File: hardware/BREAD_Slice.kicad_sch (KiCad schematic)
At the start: 29 parts, among them J1 I2C_01x04, J2 Conn_01x10_Female, K2 SANYOU_SRD_Form_C, Q1 IRLZ34N, Q2 IRLZ34N

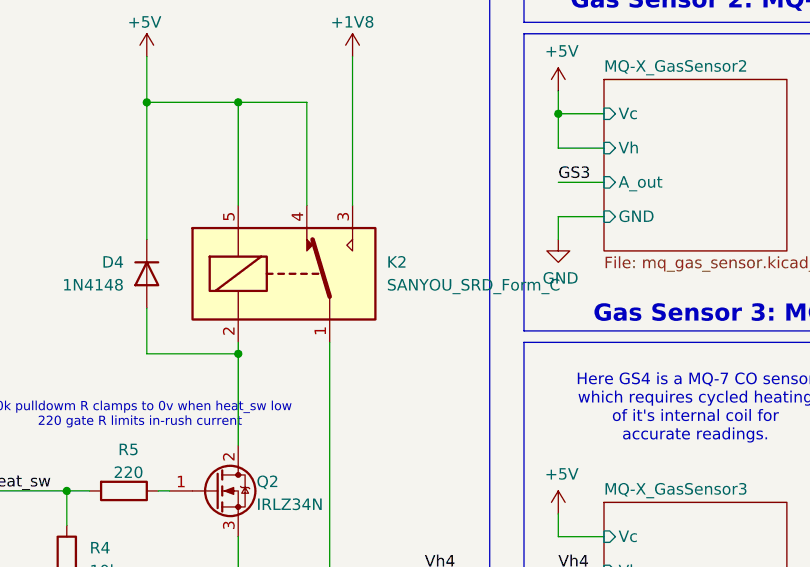
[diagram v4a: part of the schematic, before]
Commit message: updated parts list and swapped relay to omron var
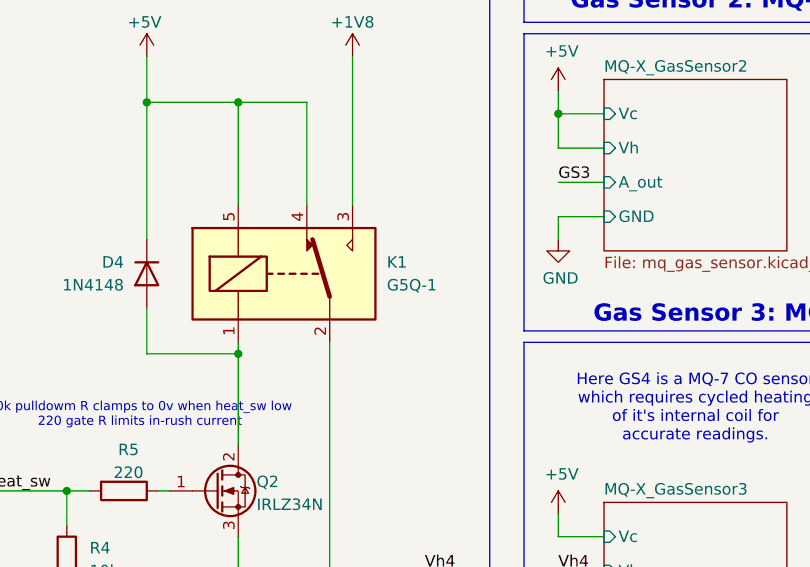
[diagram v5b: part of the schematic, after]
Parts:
- removed K2: SANYOU_SRD_Form_C, Relay_THT:Relay_SPDT_SANYOU_SRD_Series_Form_C, symbol Relay:SANYOU_SRD_Form_C
- added K1: G5Q-1, Relay_THT:Relay_SPDT_Omron-G5Q-1, symbol Relay:G5Q-1
- D2: value H178CAD -> H178CAD
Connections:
- net +1V8: now also K1.3
- net +5V: now also K1.4, K1.5
- net Vh4: now also K1.2
- net at D4.2 (A), Q2.2 (D): now also K1.1
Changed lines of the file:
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@@
+	)
+	(symbol
+		(lib_id "Relay:G5Q-1")
+		(at 217.17 109.22 0)
+		(unit 1)
+		(exclude_from_sim no)
+		(in_bom yes)
+		(on_board yes)
+		(dnp no)
+		(fields_autoplaced yes)
+		(property "Reference" "K1"
+			(at 228.6 107.9499 0)
+			(effects
+				(font
+					(size 1.27 1.27)
+				)
+				(justify left)
+			)
+		)
+		(property "Value" "G5Q-1"
+			(at 228.6 110.4899 0)
+			(effects
+				(font
+					(size 1.27 1.27)
+				)
+				(justify left)
+			)
+		)
+		(property "Footprint" "Relay_THT:Relay_SPDT_Omron-G5Q-1"
+			(at 228.6 110.49 0)
+			(effects
+				(font
+					(size 1.27 1.27)
+				)
+				(justify left)
+				(hide yes)
+			)
+		)
+		(property "Datasheet" "https://www.omron.com/ecb/products/pdf/en-g5q.pdf"
+			(at 217.17 109.22 0)
+			(effects
+				(font
+					(size 1.27 1.27)
+				)
+				(justify left)
+				(hide yes)
+			)
+		)
+		(property "Description" "Omron G5G relay, Miniature Single Pole, SPDT, 10A"
+			(at 217.17 109.22 0)
+			(effects
+				(font
+					(size 1.27 1.27)
+				)
+				(hide yes)
+			)
+		)
+		(pin "1"
+		)
+		(pin "4"
+		)
+		(pin "2"
+		)
+		(pin "3"
+		)
+		(pin "5"
+		)
+		(instances
+			(project ""
+				(path "/66043bca-a260-4915-9fce-8a51d324c687"
+					(reference "K1")
+					(unit 1)
+				)
+			)
+		)
 	)
 	(symbol
@@
 	)
 	(symbol
-		(lib_id "Relay:SANYOU_SRD_Form_C")
-		(at 217.17 109.22 0)
-		(unit 1)
-		(exclude_from_sim no)
-		(in_bom yes)
-		(on_board yes)
-		(dnp no)
-		(fields_autoplaced yes)
-		(property "Reference" "K2"
-			(at 228.6 107.9499 0)
-			(effects
-				(font
-					(size 1.27 1.27)
-				)
-				(justify left)
-			)
-		)
-		(property "Value" "SANYOU_SRD_Form_C"
-			(at 228.6 110.4899 0)
-			(effects
-				(font
-					(size 1.27 1.27)
-				)
-				(justify left)
-			)
-		)
-		(property "Footprint" "Relay_THT:Relay_SPDT_SANYOU_SRD_Series_Form_C"
-			(at 228.6 110.49 0)
-			(effects
-				(font
-					(size 1.27 1.27)
-				)
-				(justify left)
-				(hide yes)
-			)
-		)
-		(property "Datasheet" "http://www.sanyourelay.ca/public/products/pdf/SRD.pdf"
-			(at 217.17 109.22 0)
-			(effects
-				(font
-					(size 1.27 1.27)
-				)
-				(hide yes)
-			)
-		)
-		(property "Description" "Sanyo SRD relay, Single Pole Miniature Power Relay,"
-			(at 217.17 109.22 0)
-			(effects
-				(font
-					(size 1.27 1.27)
-				)
-				(hide yes)
-			)
-		)
-		(pin "4"
-		)
-		(pin "5"
-		)
-		(pin "3"
-		)
-		(pin "2"
-		)
-		(pin "1"
-		)
-		(instances
-			(project "BREAD_Slice"
-				(path "/66043bca-a260-4915-9fce-8a51d324c687"
-					(reference "K2")
-					(unit 1)
-				)
-			)
-		)
-	)
-	(symbol
 		(lib_id "Mechanical:Heatsink_Pad")
 		(at 46.99 111.76 270)
@@
 			)
 		)
-		(property "Value" "H178CAD "
+		(property "Value" "H178CAD"
 			(at 132.588 168.148 90)
 			(effects

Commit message: checked output for order
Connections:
- net Soft_CLK: now also A1.26 (A7); no longer A1.25 (A6)
- net Soft_DAT: now also A1.25 (A6); no longer A1.26 (A7)

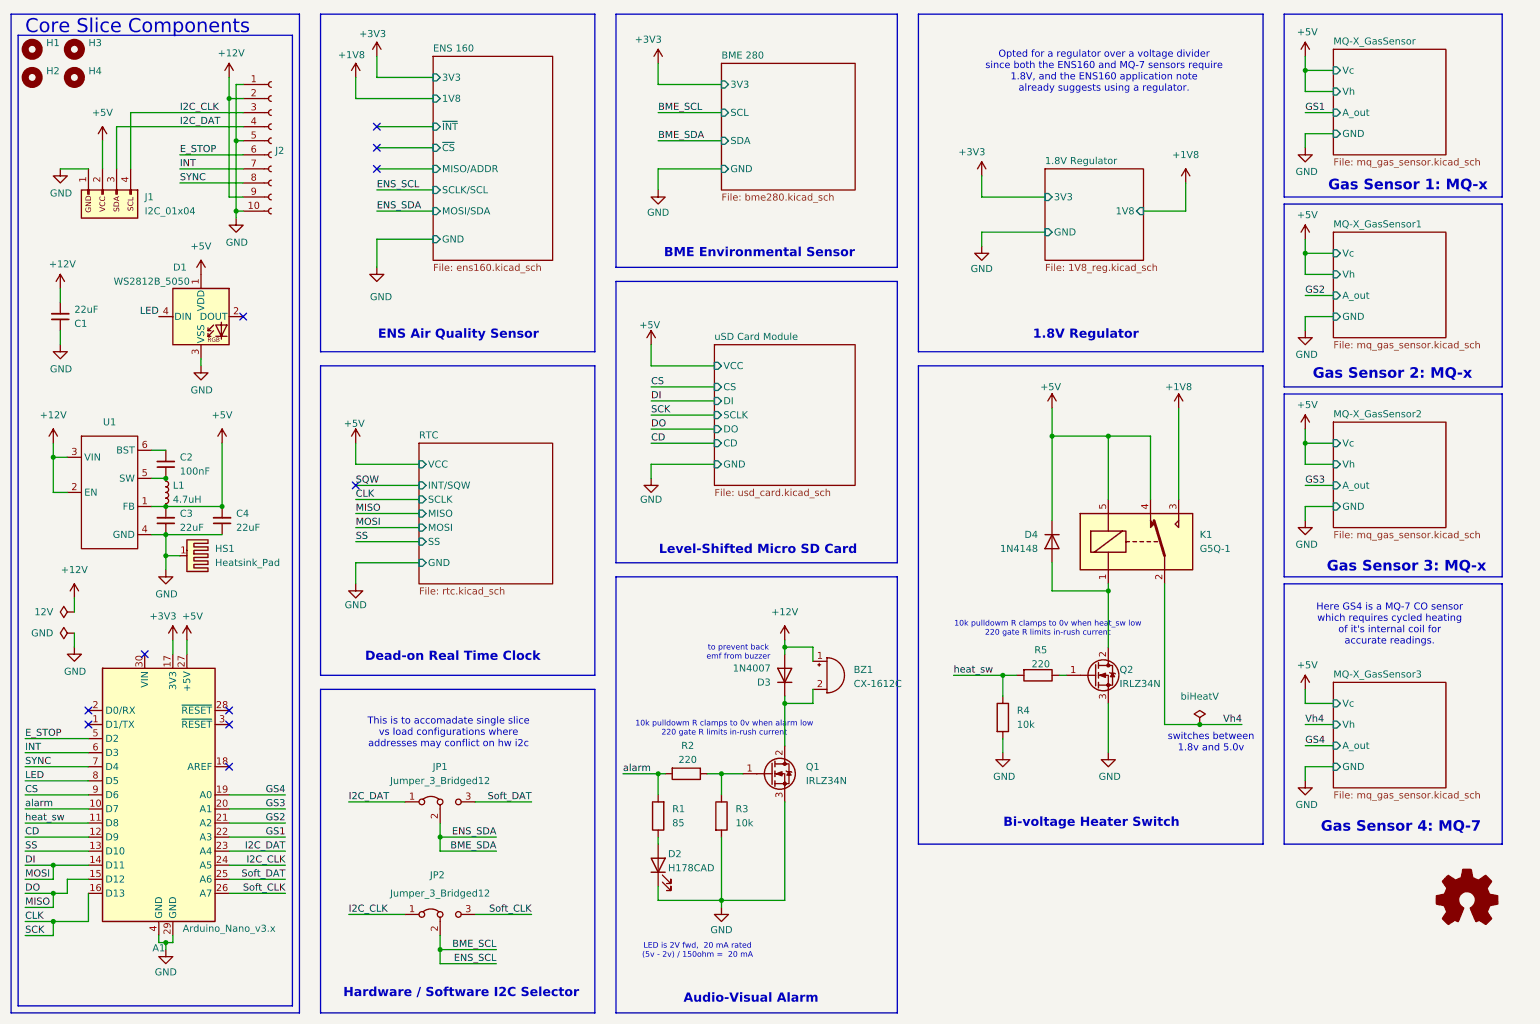
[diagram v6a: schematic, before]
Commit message: final touches for order and assembly
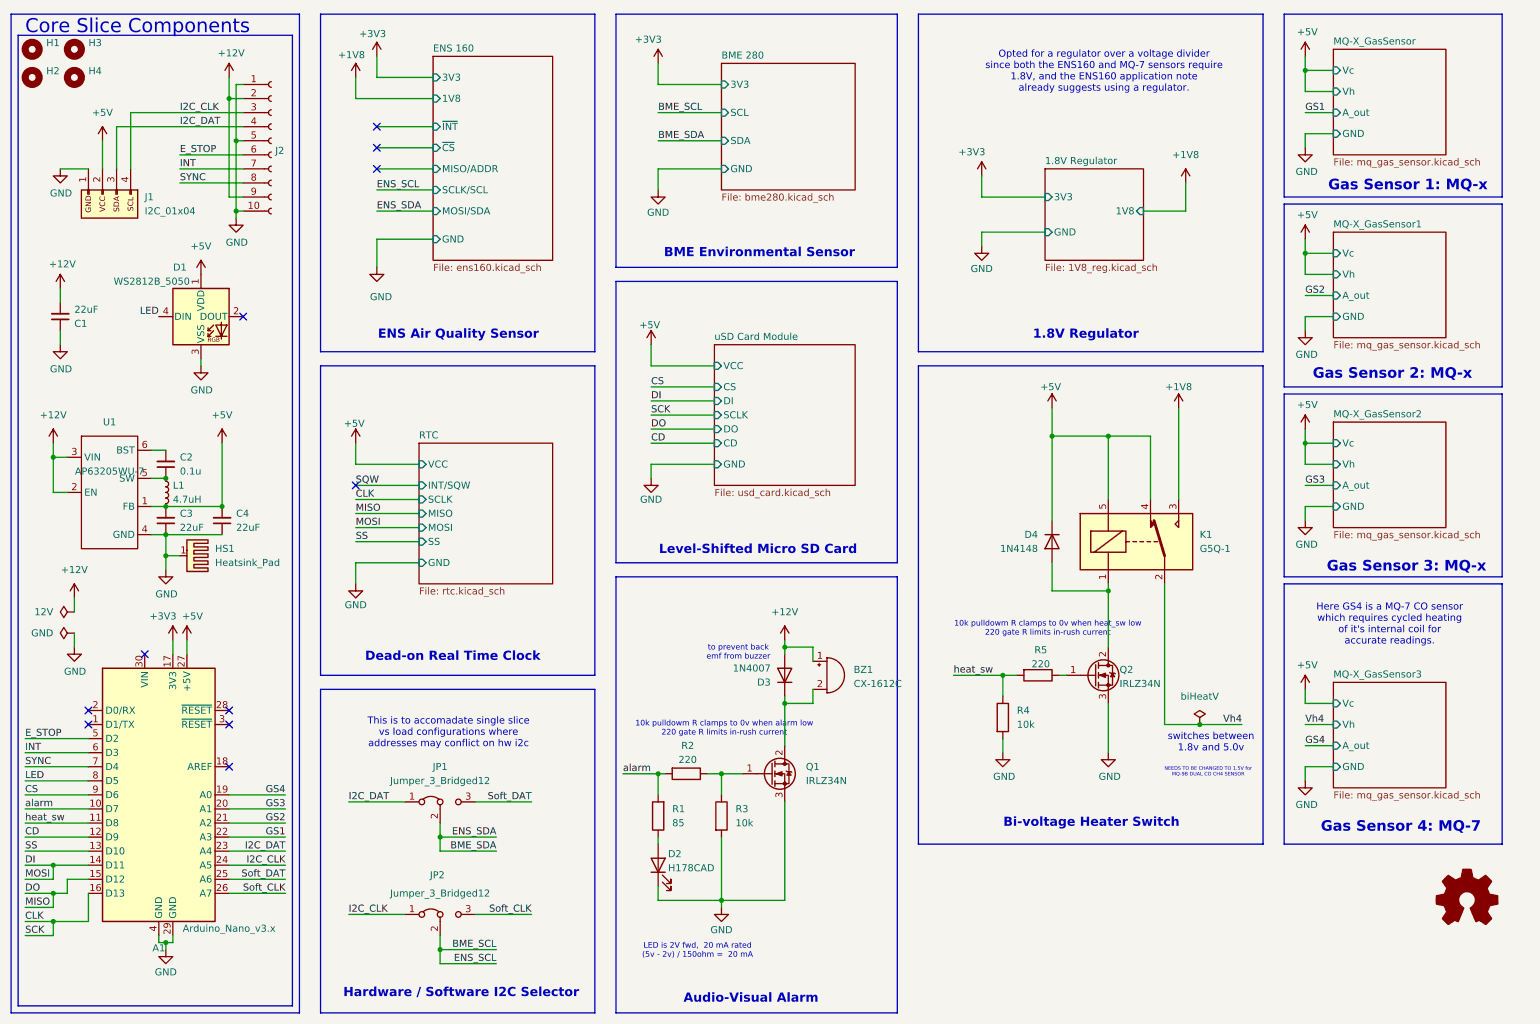
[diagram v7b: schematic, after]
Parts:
- C2: value 100nF -> 0.1u
- U1: value ~ -> AP63205WU-7
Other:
- note added: "NEEDS TO BE CHANGED TO 1.5V for MQ-9B DUAL CO CH4 SENSOR"
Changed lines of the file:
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@@
+		)
+	)
+	(text "NEEDS TO BE CHANGED TO 1.5V for \nMQ-9B DUAL CO CH4 SENSOR"
+		(exclude_from_sim no)
+		(at 230.124 150.876 0)
+		(effects
+			(font
+				(size 0.635 0.635)
+			)
 		)
 	)
@@
 		(fields_autoplaced yes)
 		(property "Reference" "C2"
-			(at 44.45 93.9736 0)
+			(at 44.45 93.9735 0)
 			(effects
 				(font
@@
 			)
 		)
-		(property "Value" "100nF"
-			(at 44.45 96.5136 0)
+		(property "Value" "0.1u"
+			(at 44.45 96.5135 0)
 			(effects
 				(font
@@
 			)
 		)
-		(property "Value" "~"
+		(property "Value" "AP63205WU-7"
 			(at 31.75 96.52 0)
 			(effects
